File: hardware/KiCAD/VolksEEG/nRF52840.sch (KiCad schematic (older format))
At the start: 30 parts, among them J2 693061010911, U2 nRF52840-Feather-Sense-Board

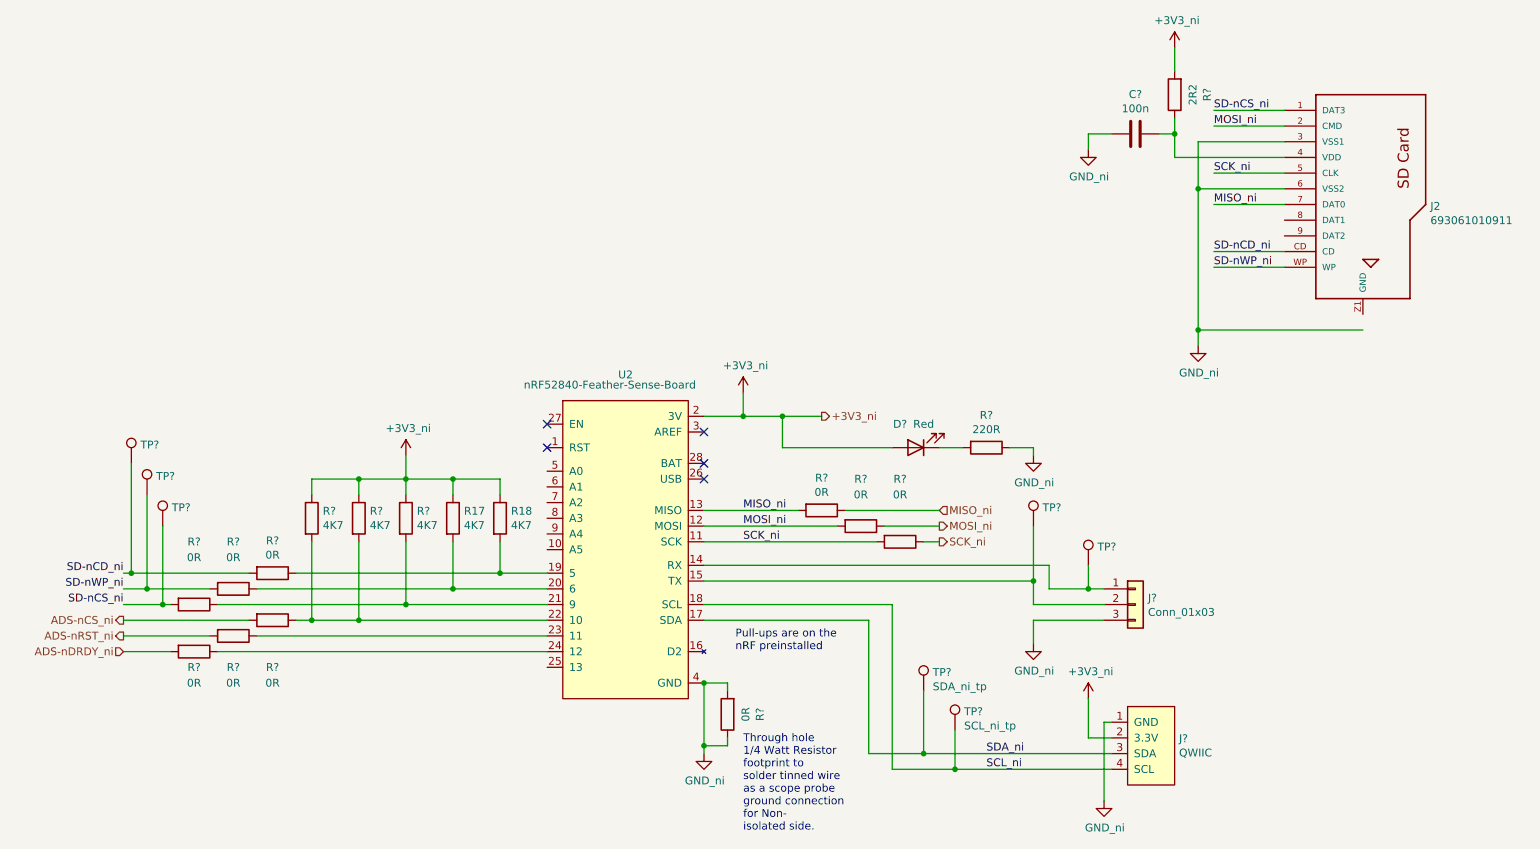
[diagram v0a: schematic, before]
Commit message: Cleaned up nrf page and converted +3V3_ni to non-global symbols.
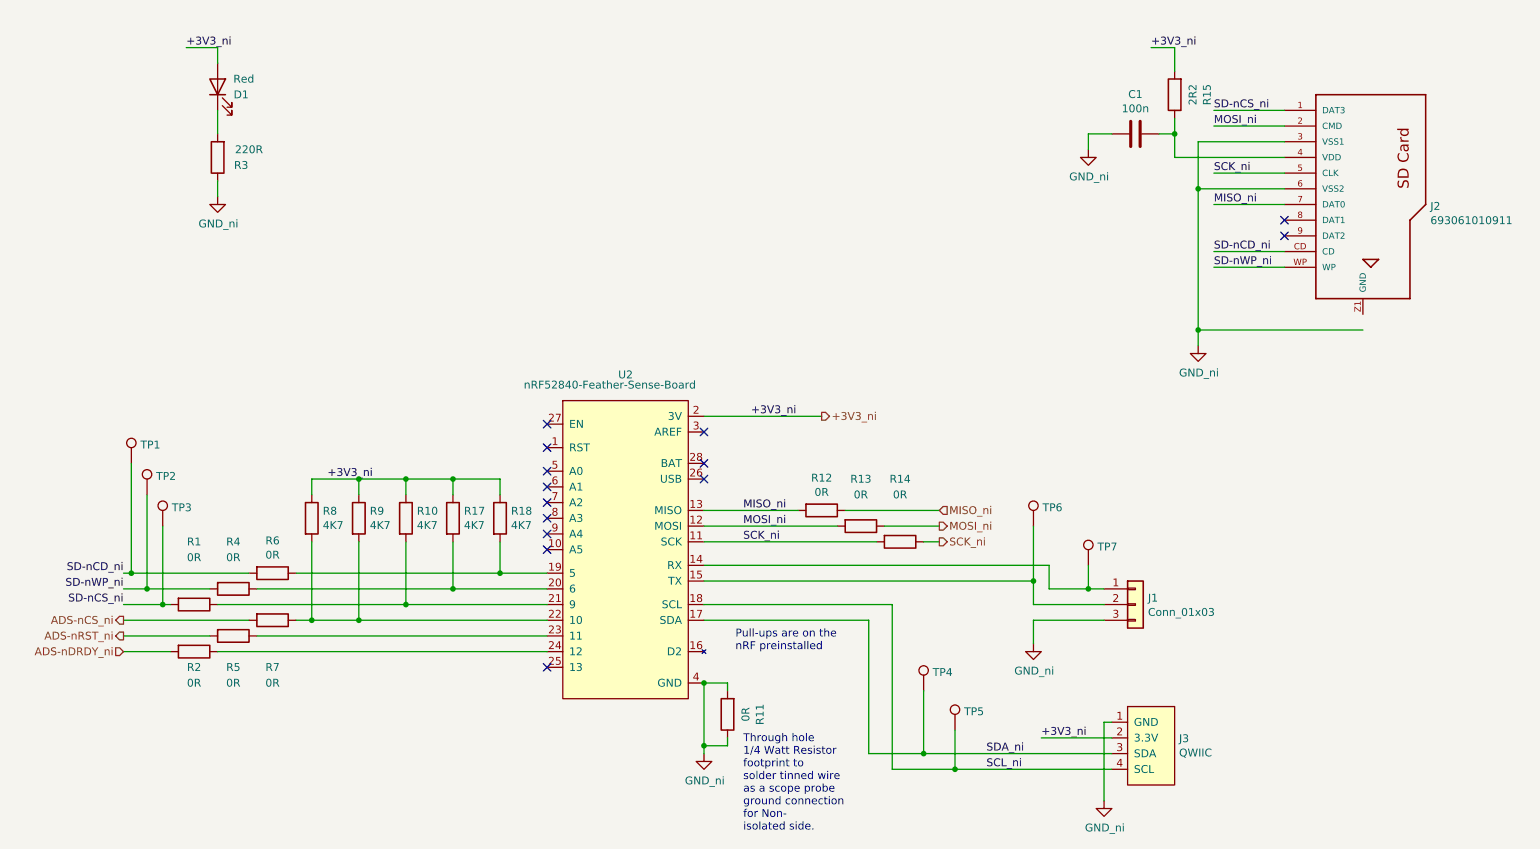
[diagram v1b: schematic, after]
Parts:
- gave numbers to parts that had none: 26
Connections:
- net +3V3 renamed +3V3_ni
- no-connect marks 5 -> 14
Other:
- moved on the sheet: D1, R3

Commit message: Annotated schematic and cleared ERC errors.
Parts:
- removed R11: 0R, symbol Device:R
- added TP31: SDA_ni_tp, symbol Connector:TestPoint
- renumbered J3 to J2, J2 to J3, R17 to R11, R18 to R12, R12 to R14, R13 to R15, R14 to R16, R15 to R17, U2 to U1
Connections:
- net GND: now also C1.1, J3.Z1 (GND), J3.Z2 (GND), TP31.1; no longer C1.2
- net at J3.4 (VDD), R17.1: now also C1.2; no longer C1.1
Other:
- note removed: "Through hole \n1/4 Watt Resistor \nfootprint to \nsolder tinned wire \nas a scope probe \nground connection\nfor Non-\nisolated side."
- moved on the sheet: C1, R17
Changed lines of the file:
@@
 NoConn ~ 5400 3500
 $Comp
-L Device:R R17
+L Device:R R11
 U 1 1 61650065
 P 3800 4050
-F 0 "R17" H 3870 4096 50  0000 L CNN
+F 0 "R11" H 3870 4096 50  0000 L CNN
 F 1 "4K7" H 3870 4005 50  0000 L CNN
 F 2 "Resistor_SMD:R_0603_1608Metric_Pad0.98x0.95mm_HandSolder" V 3730 4050 50  0001 C CNN
@@
 $EndComp
 $Comp
-L Device:R R18
+L Device:R R12
 U 1 1 6165062D
 P 4100 4050
-F 0 "R18" H 4170 4096 50  0000 L CNN
+F 0 "R12" H 4170 4096 50  0000 L CNN
 F 1 "4K7" H 4170 4005 50  0000 L CNN
 F 2 "Resistor_SMD:R_0603_1608Metric_Pad0.98x0.95mm_HandSolder" V 4030 4050 50  0001 C CNN
@@
 $EndComp
 $Comp
-L VolksEEG:QWIIC J3
+L VolksEEG:QWIIC J2
 U 1 1 6165AEA1
 P 8250 5500
-F 0 "J3" H 8428 5546 50  0000 L CNN
+F 0 "J2" H 8428 5546 50  0000 L CNN
 F 1 "QWIIC" H 8428 5455 50  0000 L CNN
 F 2 "" H 8250 5500 50  0001 C CNN
@@
 L VolksEEG:GND_ni #PWR02
 U 1 1 61BCF5D6
-P 5400 5550
-F 0 "#PWR02" H 5400 5300 50  0001 C CNN
-F 1 "GND_ni" H 5405 5377 50  0000 C CNN
-F 2 "" H 5400 5550 50  0001 C CNN
-F 3 "" H 5400 5550 50  0001 C CNN
-	1    5400 5550
-	1    0    0    -1
-$EndComp
-$Comp
-L VolksEEG:GND_ni #PWR06
+P 5650 5250
+F 0 "#PWR02" H 5650 5000 50  0001 C CNN
+F 1 "GND_ni" H 5655 5077 50  0000 C CNN
+F 2 "" H 5650 5250 50  0001 C CNN
+F 3 "" H 5650 5250 50  0001 C CNN
+	1    5650 5250
+	1    0    0    -1
+$EndComp
+$Comp
+L VolksEEG:GND_ni #PWR05
 U 1 1 61BD20F9
 P 7950 5850
-F 0 "#PWR06" H 7950 5600 50  0001 C CNN
+F 0 "#PWR05" H 7950 5600 50  0001 C CNN
 F 1 "GND_ni" H 7955 5677 50  0000 C CNN
 F 2 "" H 7950 5850 50  0001 C CNN
@@
 Wire Wire Line
 	7500 4700 7950 4700
-Wire Wire Line
-	7850 1600 8000 1600
-Wire Wire Line
-	7850 1700 7850 1600
 $Comp
 L VolksEEG:GND_ni #PWR04
 U 1 1 61DD143A
-P 7850 1700
-F 0 "#PWR04" H 7850 1450 50  0001 C CNN
-F 1 "GND_ni" H 7855 1527 50  0000 C CNN
-F 2 "" H 7850 1700 50  0001 C CNN
-F 3 "" H 7850 1700 50  0001 C CNN
-	1    7850 1700
+P 8000 2200
+F 0 "#PWR04" H 8000 1950 50  0001 C CNN
+F 1 "GND_ni" H 8005 2027 50  0000 C CNN
+F 2 "" H 8000 2200 50  0001 C CNN
+F 3 "" H 8000 2200 50  0001 C CNN
+	1    8000 2200
 	1    0    0    -1
 $EndComp
@@
 L Device:C C1
 U 1 1 61DD0AC7
-P 8150 1600
-F 0 "C1" V 7898 1600 50  0000 C CNN
-F 1 "100n" V 7989 1600 50  0000 C CNN
-F 2 "" H 8188 1450 50  0001 C CNN
-F 3 "~" H 8150 1600 50  0001 C CNN
-	1    8150 1600
-	0    1    1    0
+P 8000 2000
+F 0 "C1" V 7748 2000 50  0000 C CNN
+F 1 "100n" V 7839 2000 50  0000 C CNN
+F 2 "" H 8038 1850 50  0001 C CNN
+F 3 "~" H 8000 2000 50  0001 C CNN
+	1    8000 2000
+	-1   0    0    1
 $EndComp
 Wire Wire Line
@@
 	5400 4350 7600 4350
 $Comp
-L VolksEEG:GND_ni #PWR07
+L VolksEEG:GND_ni #PWR06
 U 1 1 61BCF9B4
 P 8550 2950
-F 0 "#PWR07" H 8550 2700 50  0001 C CNN
+F 0 "#PWR06" H 8550 2700 50  0001 C CNN
 F 1 "GND_ni" H 8555 2777 50  0000 C CNN
 F 2 "" H 8550 2950 50  0001 C CNN
@@
 Wire Wire Line
 	9600 2850 8550 2850
-Wire Wire Line
-	9100 1750 8400 1750
 Wire Wire Line
 	8550 1950 8550 2850
@@
 SD-nCS_ni
 $Comp
-L VolksEEG:693061010911 J2
+L VolksEEG:693061010911 J3
 U 1 1 6164CE12
 P 9600 1850
-F 0 "J2" H 10030 1639 50  0000 L CNN
+F 0 "J3" H 10030 1639 50  0000 L CNN
 F 1 "693061010911" H 10030 1548 50  0000 L CNN
 F 2 "VolksEEG:693061010911" H 9600 1850 50  0001 L BNN
@@
 	6300 4000 6900 4000
 $Comp
-L Device:R R13
+L Device:R R15
 U 1 1 61DF07C8
 P 6400 4100
-F 0 "R13" V 6100 4100 50  0000 C CNN
+F 0 "R15" V 6100 4100 50  0000 C CNN
 F 1 "0R" V 6200 4100 50  0000 C CNN
 F 2 "" V 6330 4100 50  0001 C CNN
@@
 	6250 4100 5400 4100
 $Comp
-L Device:R R14
+L Device:R R16
 U 1 1 61DF0A54
 P 6650 4200
-F 0 "R14" V 6250 4200 50  0000 C CNN
+F 0 "R16" V 6250 4200 50  0000 C CNN
 F 1 "0R" V 6350 4200 50  0000 C CNN
 F 2 "" V 6580 4200 50  0001 C CNN
@@
 	2550 4800 4400 4800
 $Comp
-L Device:R R12
+L Device:R R14
 U 1 1 61DF0030
 P 6150 4000
-F 0 "R12" V 5943 4000 50  0000 C CNN
+F 0 "R14" V 5943 4000 50  0000 C CNN
 F 1 "0R" V 6034 4000 50  0000 C CNN
 F 2 "" V 6080 4000 50  0001 C CNN
@@
 	7850 4500 7950 4500
 $Comp
-L Device:R R11
-U 1 1 61E287F4
-P 5550 5300
-F 0 "R11" V 5343 5300 50  0000 C CNN
-F 1 "0R" V 5434 5300 50  0000 C CNN
-F 2 "" V 5480 5300 50  0001 C CNN
-F 3 "~" H 5550 5300 50  0001 C CNN
-	1    5550 5300
-	-1   0    0    1
-$EndComp
-Wire Wire Line
-	5400 5100 5400 5500
-Wire Wire Line
-	5550 5150 5550 5100
-Wire Wire Line
-	5550 5100 5400 5100
-Connection ~ 5400 5100
-Wire Wire Line
-	5550 5450 5550 5500
-Wire Wire Line
-	5550 5500 5400 5500
-Connection ~ 5400 5500
-Wire Wire Line
-	5400 5500 5400 5550
-$Comp
 L Connector:TestPoint TP3
 U 1 1 61E37626
@@
 Wire Wire Line
 	3500 3800 3800 3800
-Wire Wire Line
-	8400 1050 8400 1200
-$Comp
-L Device:R R15
+$Comp
+L Device:R R17
 U 1 1 61E69046
-P 8400 1350
-F 0 "R15" V 8193 1350 50  0000 C CNN
-F 1 "2R2" V 8284 1350 50  0000 C CNN
-F 2 "" V 8330 1350 50  0001 C CNN
-F 3 "~" H 8400 1350 50  0001 C CNN
-	1    8400 1350
+P 8000 1550
+F 0 "R17" V 7793 1550 50  0000 C CNN
+F 1 "2R2" V 7884 1550 50  0000 C CNN
+F 2 "" V 7930 1550 50  0001 C CNN
+F 3 "~" H 8000 1550 50  0001 C CNN
+	1    8000 1550
 	-1   0    0    1
 $EndComp
-Wire Wire Line
-	8400 1500 8400 1600
-Wire Wire Line
-	8300 1600 8400 1600
-Connection ~ 8400 1600
-Wire Wire Line
-	8400 1600 8400 1750
 $Comp
 L Device:LED D1
@@
 +3V3_ni
 Wire Wire Line
-	5400 3400 6150 3400
+	5400 3400 5550 3400
 Text Label 3000 3800 0    50   ~ 0
 +3V3_ni
-Text Label 8250 1050 0    50   ~ 0
+Text Label 7850 1300 0    50   ~ 0
 +3V3_ni
 Wire Wire Line
-	8400 1050 8250 1050
+	8000 1300 7850 1300
 Text Label 2100 1050 0    50   ~ 0
 +3V3_ni
 $Comp
-L VolksEEG:nRF52840-Feather-Sense U2
+L VolksEEG:nRF52840-Feather-Sense U1
 U 1 1 6162EBF7
 P 4900 4250
-F 0 "U2" H 4900 5365 50  0000 C CNN
+F 0 "U1" H 4900 5365 50  0000 C CNN
 F 1 "nRF52840-Feather-Sense-Board" H 4800 5300 50  0000 C CNN
 F 2 "VolksEEG:nRF52840_Feather_Sense" H 4550 5250 50  0001 C CNN
@@
 NoConn ~ 4400 3850
 NoConn ~ 4400 3750
-Text Notes 5650 6050 0    50   ~ 0
-Through hole \n1/4 Watt Resistor \nfootprint to \nsolder tinned wire \nas a scope probe \nground connection\nfor Non-\nisolated side.
 NoConn ~ 9100 2250
 NoConn ~ 9100 2150
@@
 Wire Wire Line
 	7550 5450 8000 5450
+$Comp
+L Connector:TestPoint TP31
+U 1 1 619C0A65
+P 5700 5100
+F 0 "TP31" H 5758 5218 50  0000 L CNN
+F 1 "SDA_ni_tp" H 5758 5127 50  0001 L CNN
+F 2 "" H 5900 5100 50  0001 C CNN
+F 3 "~" H 5900 5100 50  0001 C CNN
+	1    5700 5100
+	0    1    1    0
+$EndComp
+Wire Wire Line
+	5700 5100 5650 5100
+Connection ~ 5650 5100
+Wire Wire Line
+	5650 5100 5650 5250
+$Comp
+L power:PWR_FLAG #FLG0101
+U 1 1 619D5B6B
+P 5550 3400
+F 0 "#FLG0101" H 5550 3475 50  0001 C CNN
+F 1 "PWR_FLAG" H 5550 3573 50  0001 C CNN
+F 2 "" H 5550 3400 50  0001 C CNN
+F 3 "~" H 5550 3400 50  0001 C CNN
+	1    5550 3400
+	1    0    0    -1
+$EndComp
+Connection ~ 5550 3400
+Wire Wire Line
+	5550 3400 6150 3400
+Wire Wire Line
+	9600 2750 9600 2850
+Wire Wire Line
+	5400 5100 5500 5100
+$Comp
+L power:PWR_FLAG #FLG0106
+U 1 1 61A08046
+P 5500 5100
+F 0 "#FLG0106" H 5500 5175 50  0001 C CNN
+F 1 "PWR_FLAG" H 5500 5273 50  0001 C CNN
+F 2 "" H 5500 5100 50  0001 C CNN
+F 3 "~" H 5500 5100 50  0001 C CNN
+	1    5500 5100
+	1    0    0    -1
+$EndComp
+Connection ~ 5500 5100
+Wire Wire Line
+	5500 5100 5650 5100
+Wire Wire Line
+	8000 1700 8000 1750
+Wire Wire Line
+	8000 1750 8000 1850
+Connection ~ 8000 1750
+Wire Wire Line
+	8000 1750 8350 1750
+Wire Wire Line
+	8000 1300 8000 1400
+Wire Wire Line
+	8000 2200 8000 2150
+$Comp
+L power:PWR_FLAG #FLG0107
+U 1 1 61A1CD95
+P 8350 1750
+F 0 "#FLG0107" H 8350 1825 50  0001 C CNN
+F 1 "PWR_FLAG" H 8350 1923 50  0001 C CNN
+F 2 "" H 8350 1750 50  0001 C CNN
+F 3 "~" H 8350 1750 50  0001 C CNN
+	1    8350 1750
+	1    0    0    -1
+$EndComp
+Connection ~ 8350 1750
+Wire Wire Line
+	8350 1750 9100 1750
 $EndSCHEMATC

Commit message: General schematic cleanup, and assigning some footprints.
Cleaning up the meta-data within KiCAD, and assigning some basic footprints.
Also, cleaning out some footprint references that didn't point anywhere.
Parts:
- C1: footprint (none) -> Capacitor_SMD:C_0603_1608Metric_Pad1.08x0.95mm_HandSolder
- R1, R14, R15, R16, R17, R2, R3, R4, R5, R6, R7: footprint (none) -> Resistor_SMD:R_0603_1608Metric_Pad0.98x0.95mm_HandSolder
- TP1: value SD-nCD_ni_tp -> TestPoint
- TP2: value SD-nWP_ni_tp -> TestPoint
- TP3: value SD-nCS_ni_tp -> TestPoint
- TP31, TP4: value SDA_ni_tp -> TestPoint
- TP5: value SCL_ni_tp -> TestPoint
- TP6: value Tx_ni_tp -> TestPoint
- TP7: value Rx_ni_tp -> TestPoint
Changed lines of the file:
@@
 F 0 "C1" V 7748 2000 50  0000 C CNN
 F 1 "100n" V 7839 2000 50  0000 C CNN
-F 2 "" H 8038 1850 50  0001 C CNN
+F 2 "Capacitor_SMD:C_0603_1608Metric_Pad1.08x0.95mm_HandSolder" H 8038 1850 50  0001 C CNN
 F 3 "~" H 8000 2000 50  0001 C CNN
 	1    8000 2000
@@
 F 0 "R15" V 6100 4100 50  0000 C CNN
 F 1 "0R" V 6200 4100 50  0000 C CNN
-F 2 "" V 6330 4100 50  0001 C CNN
+F 2 "Resistor_SMD:R_0603_1608Metric_Pad0.98x0.95mm_HandSolder" V 6330 4100 50  0001 C CNN
 F 3 "~" H 6400 4100 50  0001 C CNN
 	1    6400 4100
@@
 F 0 "R16" V 6250 4200 50  0000 C CNN
 F 1 "0R" V 6350 4200 50  0000 C CNN
-F 2 "" V 6580 4200 50  0001 C CNN
+F 2 "Resistor_SMD:R_0603_1608Metric_Pad0.98x0.95mm_HandSolder" V 6580 4200 50  0001 C CNN
 F 3 "~" H 6650 4200 50  0001 C CNN
 	1    6650 4200
@@
 F 0 "R6" V 2443 4400 50  0000 C CNN
 F 1 "0R" V 2534 4400 50  0000 C CNN
-F 2 "" V 2580 4400 50  0001 C CNN
+F 2 "Resistor_SMD:R_0603_1608Metric_Pad0.98x0.95mm_HandSolder" V 2580 4400 50  0001 C CNN
 F 3 "~" H 2650 4400 50  0001 C CNN
 	1    2650 4400
@@
 F 0 "R4" V 2100 4500 50  0000 C CNN
 F 1 "0R" V 2200 4500 50  0000 C CNN
-F 2 "" V 2330 4500 50  0001 C CNN
+F 2 "Resistor_SMD:R_0603_1608Metric_Pad0.98x0.95mm_HandSolder" V 2330 4500 50  0001 C CNN
 F 3 "~" H 2400 4500 50  0001 C CNN
 	1    2400 4500
@@
 F 0 "R1" V 1750 4600 50  0000 C CNN
 F 1 "0R" V 1850 4600 50  0000 C CNN
-F 2 "" V 2080 4600 50  0001 C CNN
+F 2 "Resistor_SMD:R_0603_1608Metric_Pad0.98x0.95mm_HandSolder" V 2080 4600 50  0001 C CNN
 F 3 "~" H 2150 4600 50  0001 C CNN
 	1    2150 4600
@@
 F 0 "R7" V 2950 4700 50  0000 C CNN
 F 1 "0R" V 3050 4700 50  0000 C CNN
-F 2 "" V 2580 4700 50  0001 C CNN
+F 2 "Resistor_SMD:R_0603_1608Metric_Pad0.98x0.95mm_HandSolder" V 2580 4700 50  0001 C CNN
 F 3 "~" H 2650 4700 50  0001 C CNN
 	1    2650 4700
@@
 F 0 "R5" V 2600 4800 50  0000 C CNN
 F 1 "0R" V 2700 4800 50  0000 C CNN
-F 2 "" V 2330 4800 50  0001 C CNN
+F 2 "Resistor_SMD:R_0603_1608Metric_Pad0.98x0.95mm_HandSolder" V 2330 4800 50  0001 C CNN
 F 3 "~" H 2400 4800 50  0001 C CNN
 	1    2400 4800
@@
 F 0 "R14" V 5943 4000 50  0000 C CNN
 F 1 "0R" V 6034 4000 50  0000 C CNN
-F 2 "" V 6080 4000 50  0001 C CNN
+F 2 "Resistor_SMD:R_0603_1608Metric_Pad0.98x0.95mm_HandSolder" V 6080 4000 50  0001 C CNN
 F 3 "~" H 6150 4000 50  0001 C CNN
 	1    6150 4000
@@
 F 0 "R2" V 2250 4900 50  0000 C CNN
 F 1 "0R" V 2350 4900 50  0000 C CNN
-F 2 "" V 2080 4900 50  0001 C CNN
+F 2 "Resistor_SMD:R_0603_1608Metric_Pad0.98x0.95mm_HandSolder" V 2080 4900 50  0001 C CNN
 F 3 "~" H 2150 4900 50  0001 C CNN
 	1    2150 4900
@@
 P 7000 5400
 F 0 "TP5" H 7058 5518 50  0000 L CNN
-F 1 "SCL_ni_tp" H 7058 5427 50  0001 L CNN
+F 1 "TestPoint" H 7058 5427 50  0001 L CNN
 F 2 "" H 7200 5400 50  0001 C CNN
 F 3 "~" H 7200 5400 50  0001 C CNN
@@
 P 6800 5150
 F 0 "TP4" H 6858 5268 50  0000 L CNN
-F 1 "SDA_ni_tp" H 6858 5177 50  0001 L CNN
+F 1 "TestPoint" H 6858 5177 50  0001 L CNN
 F 2 "" H 7000 5150 50  0001 C CNN
 F 3 "~" H 7000 5150 50  0001 C CNN
@@
 P 7850 4350
 F 0 "TP7" H 7908 4468 50  0000 L CNN
-F 1 "Rx_ni_tp" H 7908 4377 50  0001 L CNN
+F 1 "TestPoint" H 7908 4377 50  0001 L CNN
 F 2 "" H 8050 4350 50  0001 C CNN
 F 3 "~" H 8050 4350 50  0001 C CNN
@@
 P 7500 4100
 F 0 "TP6" H 7558 4218 50  0000 L CNN
-F 1 "Tx_ni_tp" H 7558 4127 50  0001 L CNN
+F 1 "TestPoint" H 7558 4127 50  0001 L CNN
 F 2 "" H 7700 4100 50  0001 C CNN
 F 3 "~" H 7700 4100 50  0001 C CNN
@@
 P 1950 4100
 F 0 "TP3" H 2008 4218 50  0000 L CNN
-F 1 "SD-nCS_ni_tp" H 2008 4127 50  0001 L CNN
+F 1 "TestPoint" H 2008 4127 50  0001 L CNN
 F 2 "" H 2150 4100 50  0001 C CNN
 F 3 "~" H 2150 4100 50  0001 C CNN
@@
 P 1850 3900
 F 0 "TP2" H 1908 4018 50  0000 L CNN
-F 1 "SD-nWP_ni_tp" H 1908 3927 50  0001 L CNN
+F 1 "TestPoint" H 1908 3927 50  0001 L CNN
 F 2 "" H 2050 3900 50  0001 C CNN
 F 3 "~" H 2050 3900 50  0001 C CNN
@@
 P 1750 3700
 F 0 "TP1" H 1808 3818 50  0000 L CNN
-F 1 "SD-nCD_ni_tp" H 1808 3727 50  0001 L CNN
+F 1 "TestPoint" H 1808 3727 50  0001 L CNN
 F 2 "" H 1950 3700 50  0001 C CNN
 F 3 "~" H 1950 3700 50  0001 C CNN
@@
 F 0 "R17" V 7793 1550 50  0000 C CNN
 F 1 "2R2" V 7884 1550 50  0000 C CNN
-F 2 "" V 7930 1550 50  0001 C CNN
+F 2 "Resistor_SMD:R_0603_1608Metric_Pad0.98x0.95mm_HandSolder" V 7930 1550 50  0001 C CNN
 F 3 "~" H 8000 1550 50  0001 C CNN
 	1    8000 1550
@@
 F 0 "R3" H 2150 1800 50  0000 C CNN
 F 1 "220R" H 2100 1700 50  0000 C CNN
-F 2 "" V 2230 1750 50  0001 C CNN
+F 2 "Resistor_SMD:R_0603_1608Metric_Pad0.98x0.95mm_HandSolder" V 2230 1750 50  0001 C CNN
 F 3 "~" H 2300 1750 50  0001 C CNN
 	1    2300 1750
@@
 P 5700 5100
 F 0 "TP31" H 5758 5218 50  0000 L CNN
-F 1 "SDA_ni_tp" H 5758 5127 50  0001 L CNN
+F 1 "TestPoint" H 5758 5127 50  0001 L CNN
 F 2 "" H 5900 5100 50  0001 C CNN
 F 3 "~" H 5900 5100 50  0001 C CNN
